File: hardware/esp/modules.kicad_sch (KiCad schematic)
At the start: 40 parts, among them J5 Conn_01x09_Pin, J6 Conn_01x09_Pin, U3 VL53L0X, U4 NRF24L01, U5 BME280, Y1 16MHz

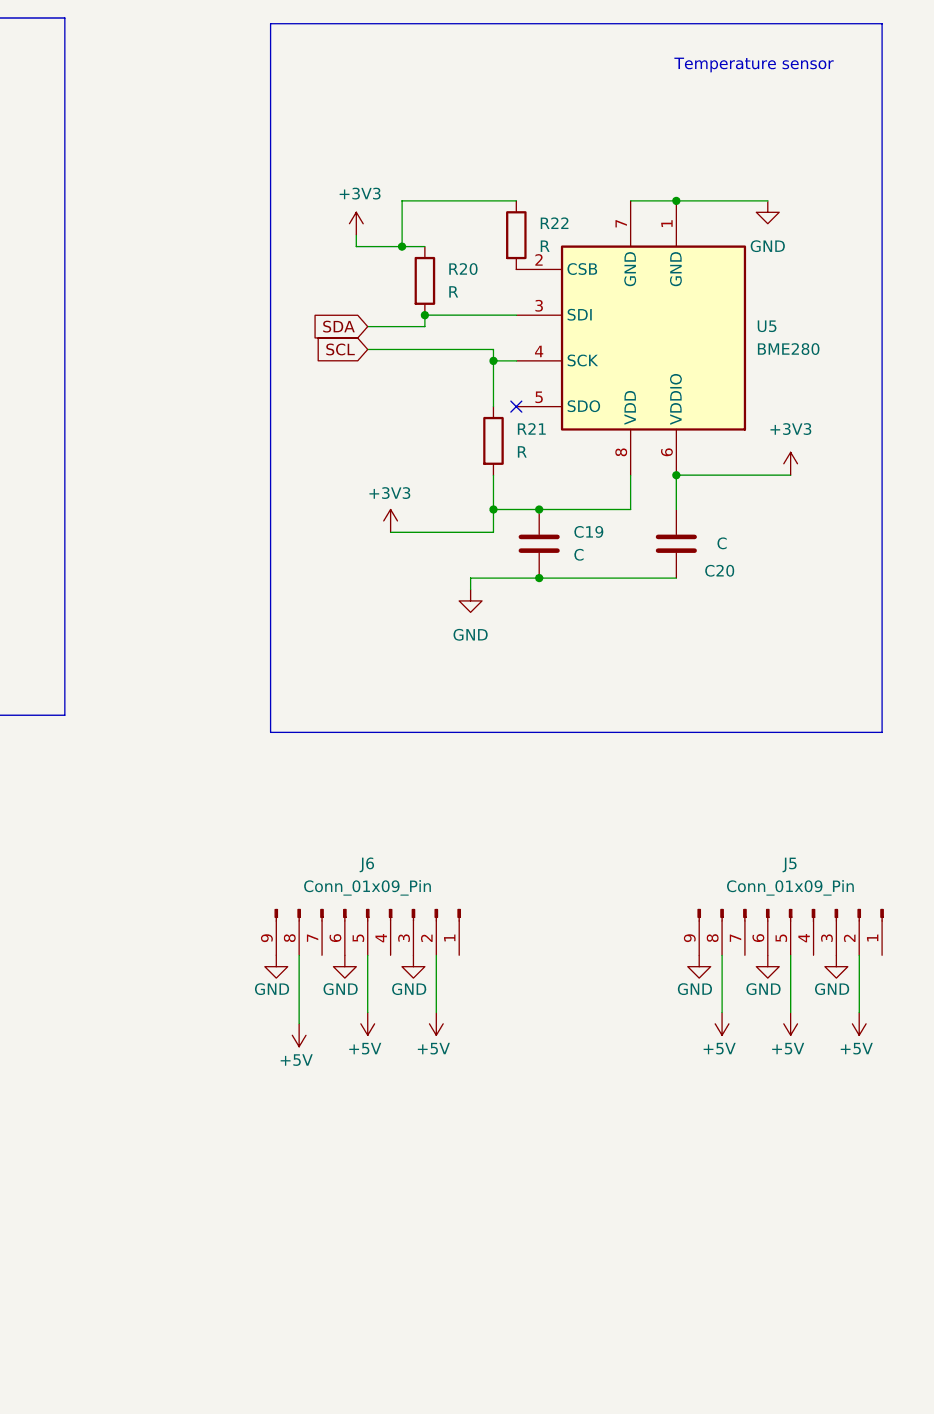
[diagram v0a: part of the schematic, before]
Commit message: Updating pins, working on schematic and placing components on PCB
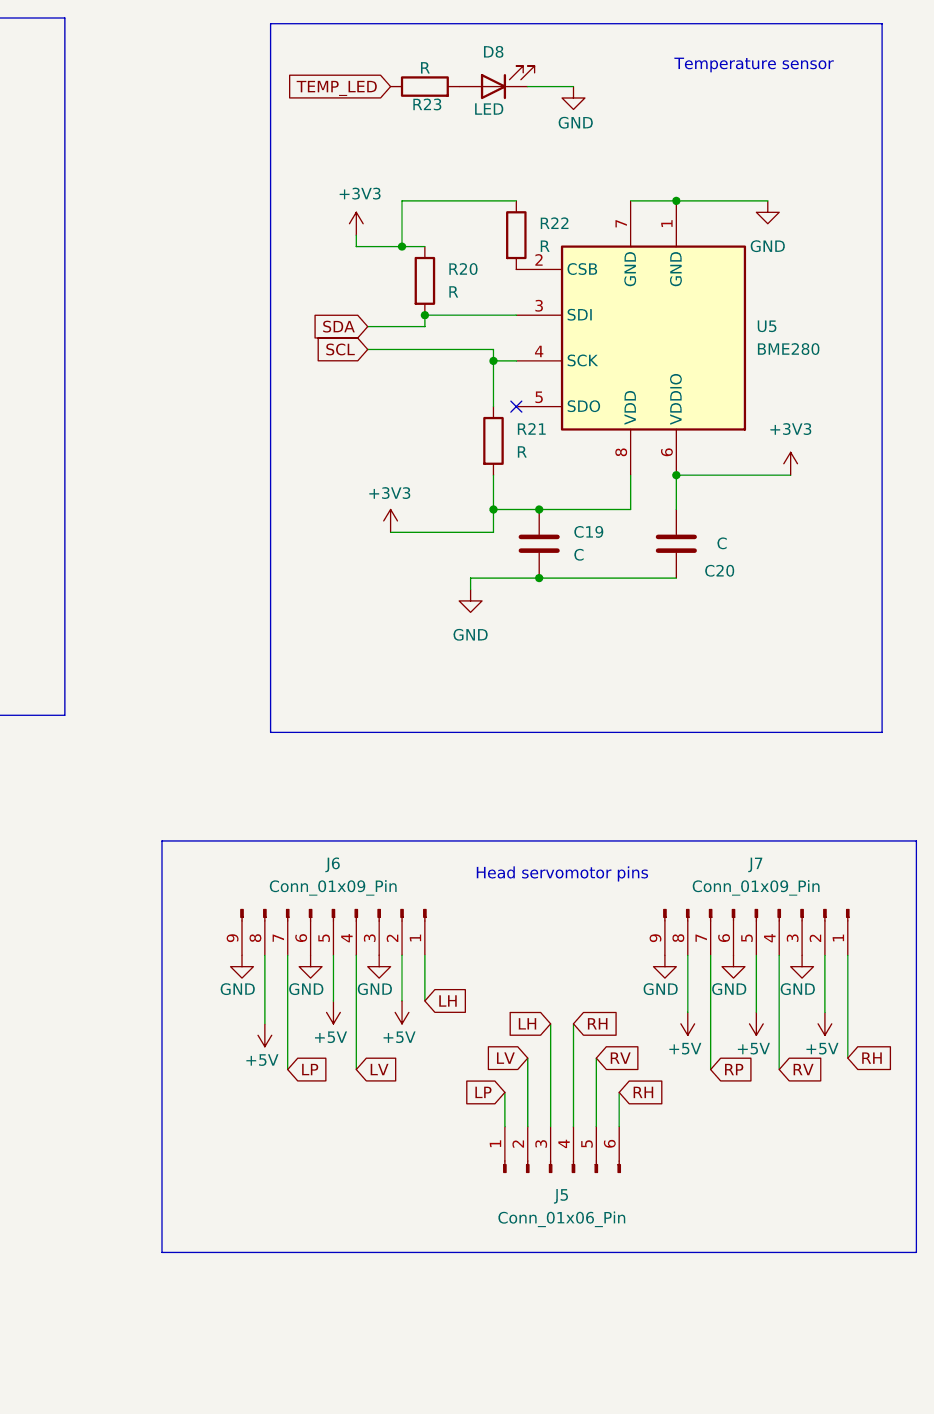
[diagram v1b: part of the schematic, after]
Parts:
- removed J5: Conn_01x09_Pin, Connector_PinHeader_2.54mm:PinHeader_1x09_P2.54mm_Vertical, symbol Connector:Conn_01x09_Pin
- added D8: LED, LED_SMD:LED_0603_1608Metric, symbol Device:LED
- added J5: Conn_01x06_Pin, Connector_PinHeader_2.54mm:PinHeader_1x06_P2.54mm_Horizontal, symbol Connector:Conn_01x06_Pin
- added J7: Conn_01x09_Pin, Connector_PinHeader_2.54mm:PinHeader_1x09_P2.54mm_Vertical, symbol Connector:Conn_01x09_Pin
- added R23: R, Resistor_SMD:R_0805_2012Metric, symbol Device:R
- U3: PURCHASE-URL (none) -> https://www.snapeda.com/api/url_track_click_mouser/?unipart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; Purchase-URL https://www.snapeda.com/api/url_track_click_mouser/?unipart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 -> (none)
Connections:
- net +5V: now also J7.2 (Pin_2), J7.5 (Pin_5), J7.8 (Pin_8)
- net GND: now also D8.1 (K), J7.3 (Pin_3), J7.6 (Pin_6), J7.9 (Pin_9)
- net LH: now reaches J6.1 (Pin_1)
- net LH: now also J5.3 (Pin_3)
- net LV: now reaches J6.4 (Pin_4)
- net LV: now also J5.2 (Pin_2)
- net LP: now reaches J6.7 (Pin_7)
- net LP: now also J5.1 (Pin_1)
- new net: D8.2 (A), R23.2
- new net RH: J5.4 (Pin_4), J5.6 (Pin_6), J7.1 (Pin_1)
- new net RP: J7.7 (Pin_7)
- new net RV: J5.5 (Pin_5), J7.4 (Pin_4)
- new net TEMP_LED: R23.1
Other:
- note added: "Head servomotor pins"

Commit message: Updating schematics and PCB layout
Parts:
- removed R17, R18: 1.5K, Resistor_SMD:R_0805_2012Metric, symbol Device:R
- removed R22: R, Resistor_SMD:R_0805_2012Metric, symbol Device:R
- C11, C14, C16: footprint Capacitor_SMD:C_0603_1608Metric -> Capacitor_SMD:C_0805_2012Metric
- C19, C20: value C -> 0.1uF; footprint Capacitor_SMD:C_0603_1608Metric -> Capacitor_SMD:C_0805_2012Metric
- R14, R15: value 1.5K -> 4.7k
- R20, R21: value R -> 4.7k
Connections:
- net XSHUT is gone; now on net +3V3: U3.5 (~{XSHUT})
- net +3V3: now also U5.2 (CSB)
- net DIST_GPIO1: no longer names the net of U3.7 (GPIO1)
- no-connect marks 2 -> 3

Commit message: Placing components on PCB and starting routing
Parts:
- L3: value 2.7nH -> 3.9nH
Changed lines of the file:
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@@
 			)
 		)
-		(property "Value" "2.7nH"
+		(property "Value" "3.9nH"
 			(at 128.016 38.862 90)
 			(show_name no)

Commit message: Updating pins, and scehmatic
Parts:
- removed AE1: Antenna, symbol Device:Antenna
- added J5: Conn_Coaxial, Connector_Coaxial:U.FL_Molex_MCRF_73412-0110_Vertical, symbol Connector:Conn_Coaxial
- renumbered C8 to C12, C9 to C13, C10 to C14, C11 to C15, C12 to C16, C13 to C17, C14 to C18, C15 to C19, C16 to C20, C17 to C21, C18 to C22, C19 to C23, C20 to C24, D4 to D5, D5 to D6, D6 to D7, D7 to D8, D8 to D9, J5 to J7, J7 to J8, R10 to R11, R11 to R12, R12 to R13, R13 to R14, R14 to R15, R15 to R16, R16 to R17, R19 to R18, R23 to R19, U3 to U4, U4 to U5, U5 to U6
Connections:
- net GND: now also J5.2 (Ext)
- net at C21.2, C22.2: now also J5.1 (In)

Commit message: Fixing schematic error and routing PCB
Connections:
- net RH: no longer J7.6 (Pin_6)
- net RP: now also J7.6 (Pin_6)

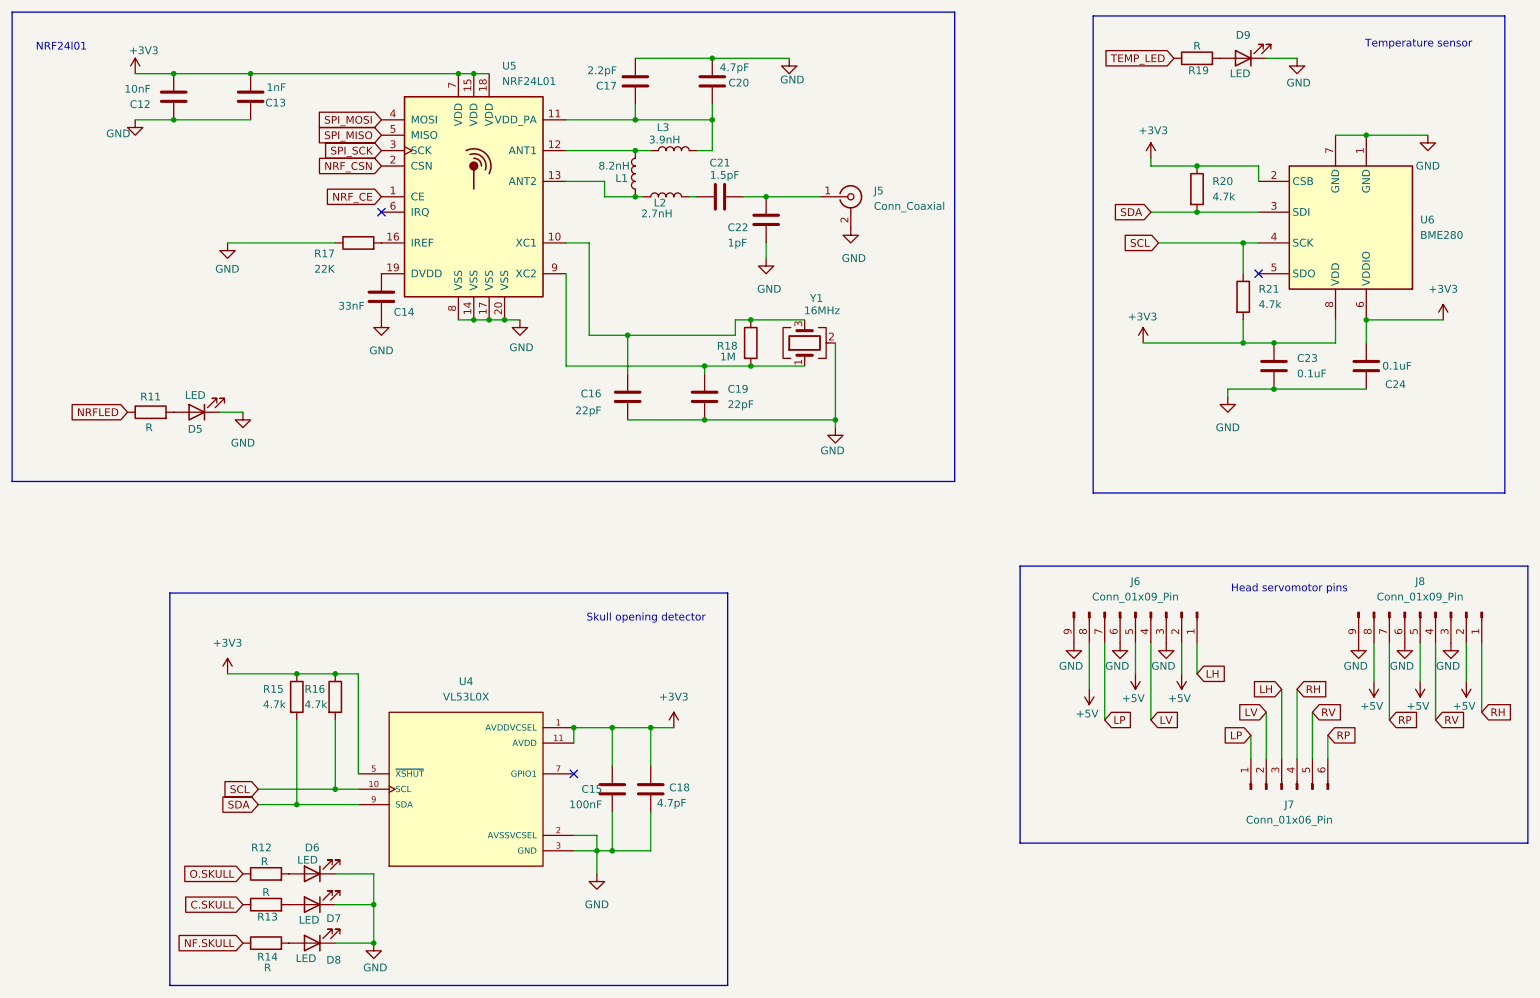
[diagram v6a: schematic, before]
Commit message: Modifiying schematic after schematic review
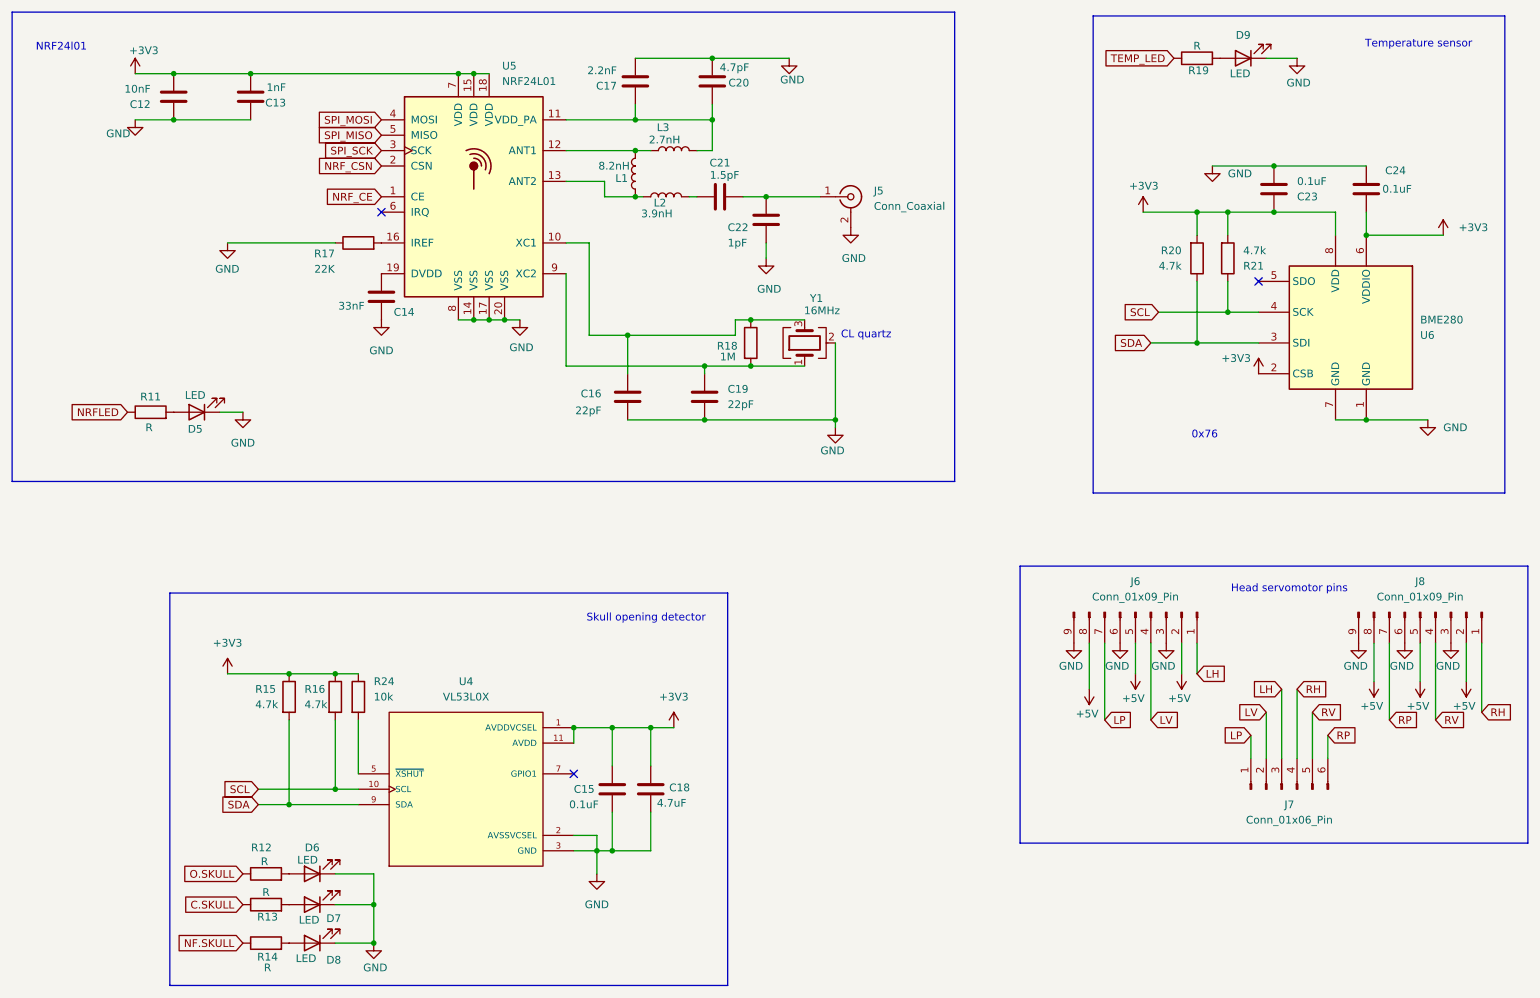
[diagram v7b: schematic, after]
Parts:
- added R24: 10k, symbol Device:R
- C15: value 100nF -> 0.1uF
- C17: value 2.2pF -> 2.2nF
- C18: value 4.7pF -> 4.7uF
- L2: value 2.7nH -> 3.9nH
- L3: value 3.9nH -> 2.7nH
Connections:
- net +3V3: now also R20.2, R24.1; no longer R20.1, U4.5 (~{XSHUT})
- net SDA: now also R20.1; no longer R20.2
- new net: R24.2, U4.5 (~{XSHUT})
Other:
- note added: "0x76"
- note added: "CL quartz"
- moved on the sheet: C23, C24, R15, R20, R21, U6

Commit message: Updating schemaitc, and component placement on PCB
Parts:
- R24: footprint (none) -> Resistor_SMD:R_0805_2012Metric
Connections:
- net +3V3: now also C24.2; no longer C24.1
- net GND: now also C24.1; no longer C24.2
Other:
- note added: "(skull opening detection)"
- note added: "0x29"
- note added: "2.4GHz Transreceiver"
- note added: "Distance sensor"
- note removed: "NRF24l01"
- note removed: "Skull opening detector"
- moved on the sheet: C24
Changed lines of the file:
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@@
 		)
 	)
+	(text "(skull opening detection)"
+		(exclude_from_sim no)
+		(at 122.936 120.65 0)
+		(effects
+			(font
+				(size 1.27 1.27)
+			)
+		)
+	)
 	(text "0x76"
 		(exclude_from_sim no)
@@
 		)
 	)
-	(text "NRF24l01"
+	(text "2.4GHz Transreceiver"
 		(exclude_from_sim no)
-		(at 28.448 23.622 0)
+		(at 36.576 50.292 0)
 		(effects
 			(font
@@
 		)
 	)
-	(text "Skull opening detector"
+	(text "0x29"
 		(exclude_from_sim no)
-		(at 124.968 117.856 0)
+		(at 106.426 172.72 0)
+		(effects
+			(font
+				(size 1.27 1.27)
+			)
+		)
+	)
+	(text "Distance sensor"
+		(exclude_from_sim no)
+		(at 122.428 118.11 0)
 		(effects
 			(font
@@
 	)
 	(junction
-		(at 243.84 54.61)
-		(diameter 0)
-		(color 0 0 0 0)
-	)
-	(junction
 		(at 66.04 127)
 		(diameter 0)
@@
 	)
 	(junction
-		(at 80.01 165.1)
+		(at 243.84 50.8)
 		(diameter 0)
 		(color 0 0 0 0)
 	)
 	(junction
-		(at 46.99 35.56)
+		(at 80.01 165.1)
 		(diameter 0)
 		(color 0 0 0 0)
 	)
 	(junction
-		(at 135.89 25.4)
+		(at 46.99 35.56)
 		(diameter 0)
 		(color 0 0 0 0)
 	)
 	(junction
-		(at 228.6 43.18)
+		(at 135.89 25.4)
 		(diameter 0)
 		(color 0 0 0 0)
@@
 	(wire
 		(pts
-			(xy 243.84 54.61) (xy 256.54 54.61)
-		)
-		(stroke
-			(width 0)
-			(type default)
-		)
-	)
-	(wire
-		(pts
 			(xy 139.7 71.12) (xy 139.7 68.58)
 		)
@@
 	(wire
 		(pts
-			(xy 243.84 54.61) (xy 243.84 50.8)
-		)
-		(stroke
-			(width 0)
-			(type default)
-		)
-	)
-	(wire
-		(pts
 			(xy 60.96 146.05) (xy 73.66 146.05)
 		)
@@
 	(wire
 		(pts
+			(xy 243.84 50.8) (xy 243.84 54.61)
+		)
+		(stroke
+			(width 0)
+			(type default)
+		)
+	)
+	(wire
+		(pts
 			(xy 80.01 165.1) (xy 80.01 171.45)
 		)
@@
 	(wire
 		(pts
+			(xy 243.84 43.18) (xy 243.84 50.8)
+		)
+		(stroke
+			(width 0)
+			(type default)
+		)
+	)
+	(wire
+		(pts
 			(xy 215.9 50.8) (xy 220.98 50.8)
 		)
@@
 	(wire
 		(pts
+			(xy 255.27 50.8) (xy 251.46 50.8)
+		)
+		(stroke
+			(width 0)
+			(type default)
+		)
+	)
+	(wire
+		(pts
 			(xy 66.04 148.59) (xy 77.47 148.59)
 		)
@@
 	(wire
 		(pts
-			(xy 228.6 43.18) (xy 243.84 43.18)
-		)
-		(stroke
-			(width 0)
-			(type default)
-		)
-	)
-	(wire
-		(pts
 			(xy 58.42 83.82) (xy 54.61 83.82)
 		)
@@
 	)
 	(symbol
+		(lib_id "power:GND")
+		(at 255.27 50.8 0)
+		(mirror y)
+		(unit 1)
+		(body_style 1)
+		(exclude_from_sim no)
+		(in_bom yes)
+		(on_board yes)
+		(in_pos_files yes)
+		(dnp no)
+		(fields_autoplaced yes)
+		(property "Reference" "#PWR057"
+			(at 255.27 57.15 0)
+			(hide yes)
+			(show_name no)
+			(do_not_autoplace no)
+			(effects
+				(font
+					(size 1.27 1.27)
+				)
+			)
+		)
+		(property "Value" "GND"
+			(at 257.81 52.0699 0)
+			(show_name no)
+			(do_not_autoplace no)
+			(effects
+				(font
+					(size 1.27 1.27)
+				)
+				(justify right)
+			)
+		)
+		(property "Footprint" ""
+			(at 255.27 50.8 0)
+			(hide yes)
+			(show_name no)
+			(do_not_autoplace no)
+			(effects
+				(font
+					(size 1.27 1.27)
+				)
+			)
+		)
+		(property "Datasheet" ""
+			(at 255.27 50.8 0)
+			(hide yes)
+			(show_name no)
+			(do_not_autoplace no)
+			(effects
+				(font
+					(size 1.27 1.27)
+				)
+			)
+		)
+		(property "Description" "Power symbol creates a global label with name \"GND\" , ground"
+			(at 255.27 50.8 0)
+			(hide yes)
+			(show_name no)
+			(do_not_autoplace no)
+			(effects
+				(font
+					(size 1.27 1.27)
+				)
+			)
+		)
+		(pin "1"
+		)
+		(instances
+			(project "esp"
+				(path "/44c5117f-5e76-477e-b7df-13896ca2c21f"
+					(reference "#PWR057")
+					(unit 1)
+				)
+			)
+		)
+	)
+	(symbol
 		(lib_id "power:+3V3")
 		(at 129.54 135.89 0)
@@
 	(symbol
 		(lib_id "Device:C")
-		(at 243.84 46.99 0)
+		(at 247.65 50.8 270)
 		(mirror x)
 		(unit 1)
@@
 		(dnp no)
 		(property "Reference" "C24"
-			(at 248.666 43.942 0)
+			(at 248.412 57.912 90)
 			(show_name no)
 			(do_not_autoplace no)
@@
 		)
 		(property "Value" "0.1uF"
-			(at 248.92 46.99 0)
+			(at 248.158 54.864 90)
 			(show_name no)
 			(do_not_autoplace no)
@@
 		)
 		(property "Footprint" "Capacitor_SMD:C_0805_2012Metric"
-			(at 244.8052 43.18 0)
+			(at 243.84 49.8348 0)
 			(hide yes)
 			(show_name no)
@@
 		)
 		(property "Datasheet" ""
-			(at 243.84 46.99 0)
+			(at 247.65 50.8 0)
 			(hide yes)
 			(show_name no)
@@
 		)
 		(property "Description" "Unpolarized capacitor"
-			(at 243.84 46.99 0)
+			(at 247.65 50.8 0)
 			(hide yes)
 			(show_name no)
@@
 		)
 		(property "MAXIMUM_PACKAGE_HEIGHT" ""
-			(at 243.84 46.99 0)
+			(at 247.65 50.8 0)
 			(hide yes)
 			(show_name no)
@@
 		)
 		(property "PARTREV" ""
-			(at 243.84 46.99 0)
+			(at 247.65 50.8 0)
 			(hide yes)
 			(show_name no)
@@
 		)
 		(property "SNAPEDA_PACKAGE_ID" ""
-			(at 243.84 46.99 0)
+			(at 247.65 50.8 0)
 			(hide yes)
 			(show_name no)
@@
 		)
 		(property "Sim.Device" ""
-			(at 243.84 46.99 0)
+			(at 247.65 50.8 0)
 			(hide yes)
 			(show_name no)
@@
 		)
 		(property "Sim.Type" ""
-			(at 243.84 46.99 0)
+			(at 247.65 50.8 0)
 			(hide yes)
 			(show_name no)
@@
 			)
 		)
-		(property "Footprint" ""
+		(property "Footprint" "Resistor_SMD:R_0805_2012Metric"
 			(at 75.692 130.81 90)
 			(hide yes)
@@
 	(symbol
 		(lib_id "power:+3V3")
-		(at 256.54 54.61 0)
+		(at 243.84 43.18 0)
 		(mirror y)
 		(unit 1)
@@
 		(fields_autoplaced yes)
 		(property "Reference" "#PWR052"
-			(at 256.54 58.42 0)
+			(at 243.84 46.99 0)
 			(hide yes)
 			(show_name no)
@@
 		)
 		(property "Value" "+3V3"
-			(at 259.08 53.3399 0)
+			(at 246.38 41.9099 0)
 			(show_name no)
 			(do_not_autoplace no)
@@
 		)
 		(property "Footprint" ""
-			(at 256.54 54.61 0)
+			(at 243.84 43.18 0)
 			(hide yes)
 			(show_name no)
@@
 		)
 		(property "Datasheet" ""
-			(at 256.54 54.61 0)
+			(at 243.84 43.18 0)
 			(hide yes)
 			(show_name no)
@@
 		)
 		(property "Description" "Power symbol creates a global label with name \"+3V3\""
-			(at 256.54 54.61 0)
+			(at 243.84 43.18 0)
 			(hide yes)
 			(show_name no)
@@
 		)
 	)
+	(embedded_fonts no)
 )
